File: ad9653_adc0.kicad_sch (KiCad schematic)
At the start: 20 parts, among them J201 142-0701-201, J202 142-0701-201, J203 142-0701-201, J204 142-0701-201, U201 AD9653BCPZ-125

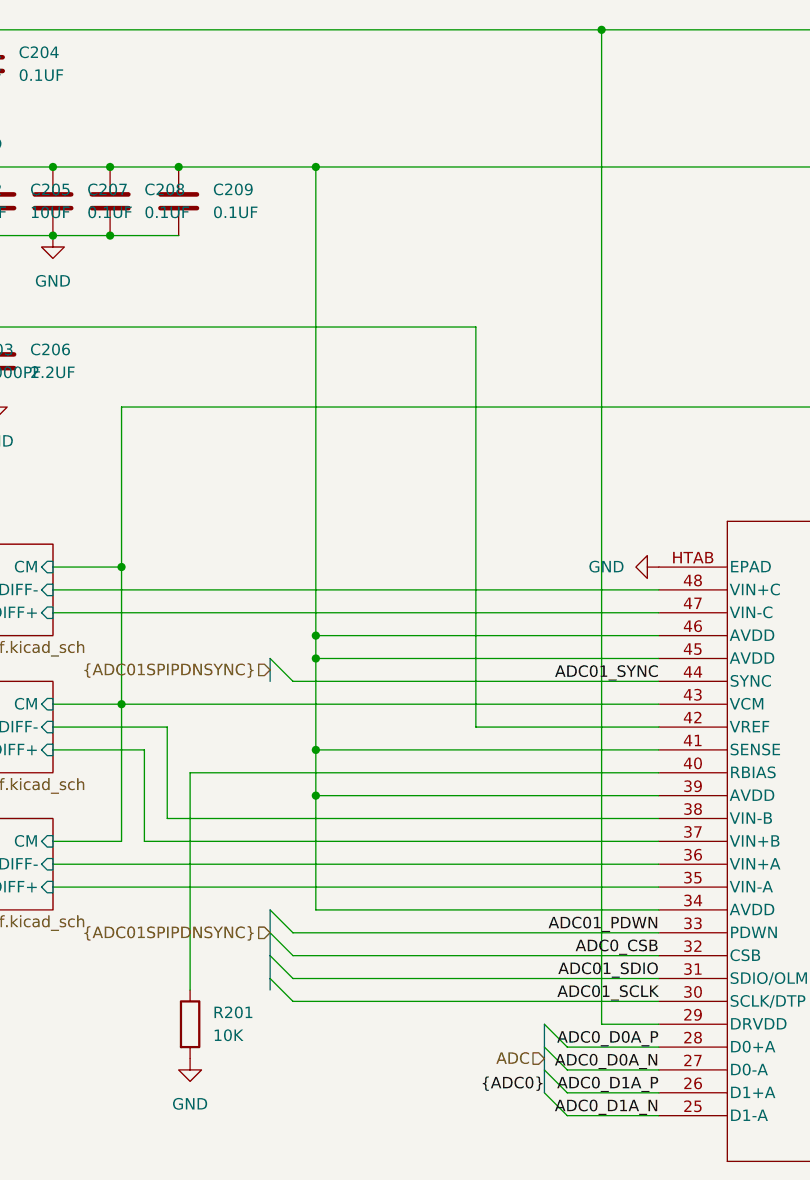
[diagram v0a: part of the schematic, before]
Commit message: Updates from Michal to fix ERC errors
Still lots of ERC warnings
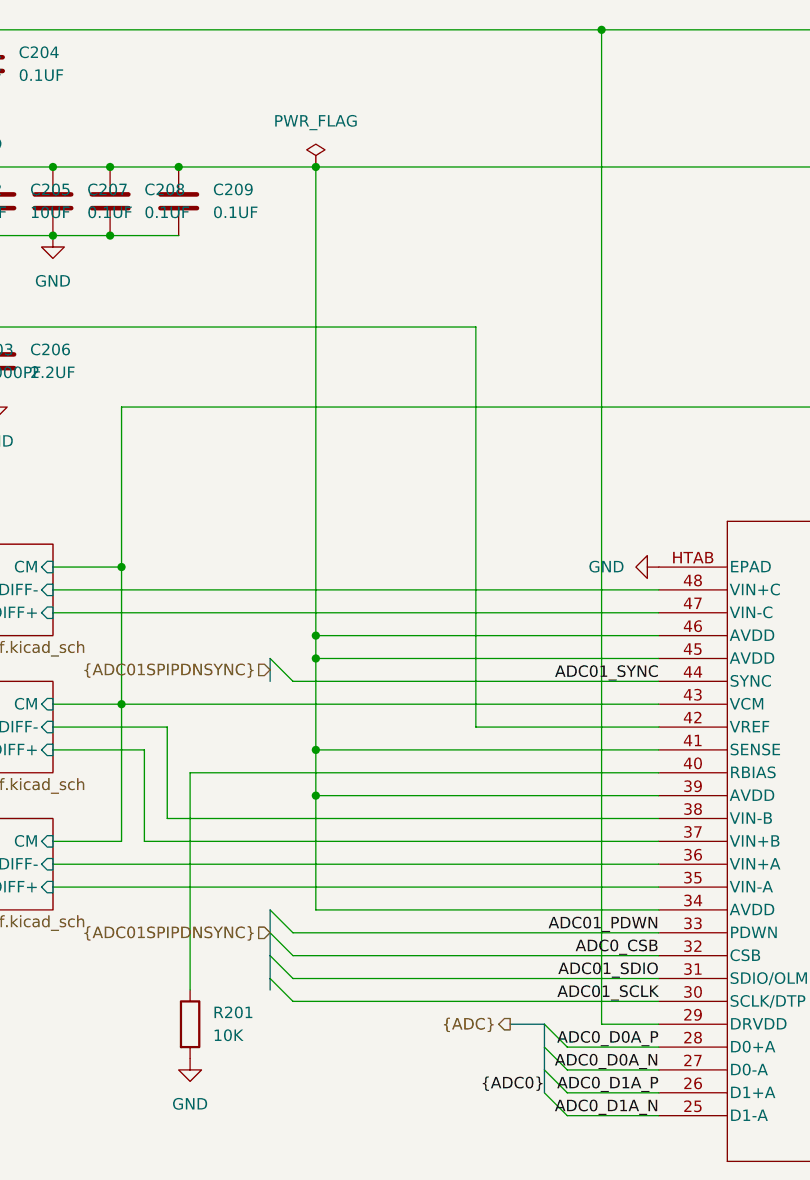
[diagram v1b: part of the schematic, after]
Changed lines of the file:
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@@
+		)
+	)
+	(bus
+		(pts
+			(xy 115.57 137.16) (xy 115.57 139.7)
+		)
+		(stroke
+			(width 0)
+			(type default)
 		)
 	)
@@
 	(bus
 		(pts
+			(xy 115.57 134.62) (xy 115.57 137.16)
+		)
+		(stroke
+			(width 0)
+			(type default)
+		)
+	)
+	(bus
+		(pts
 			(xy 233.68 121.92) (xy 233.68 124.46)
 		)
@@
 		)
 	)
+	(wire
+		(pts
+			(xy 200.66 39.37) (xy 90.17 39.37)
+		)
+		(stroke
+			(width 0)
+			(type default)
+		)
+	)
+	(wire
+		(pts
+			(xy 199.39 109.22) (xy 231.14 109.22)
+		)
+		(stroke
+			(width 0)
+			(type default)
+		)
+	)
+	(wire
+		(pts
+			(xy 238.76 66.04) (xy 238.76 81.28)
+		)
+		(stroke
+			(width 0)
+			(type default)
+		)
+	)
+	(wire
+		(pts
+			(xy 87.63 124.46) (xy 128.27 124.46)
+		)
+		(stroke
+			(width 0)
+			(type default)
+		)
+	)
+	(wire
+		(pts
+			(xy 76.2 106.68) (xy 76.2 130.81)
+		)
+		(stroke
+			(width 0)
+			(type default)
+		)
+	)
+	(wire
+		(pts
+			(xy 219.71 99.06) (xy 234.95 99.06)
+		)
+		(stroke
+			(width 0)
+			(type default)
+		)
+	)
+	(wire
+		(pts
+			(xy 60.96 114.3) (xy 68.58 114.3)
+		)
+		(stroke
+			(width 0)
+			(type default)
+		)
+	)
+	(wire
+		(pts
+			(xy 60.96 46.99) (xy 67.31 46.99)
+		)
+		(stroke
+			(width 0)
+			(type default)
+		)
+	)
+	(wire
+		(pts
+			(xy 87.63 129.54) (xy 128.27 129.54)
+		)
+		(stroke
+			(width 0)
+			(type default)
+		)
+	)
+	(wire
+		(pts
+			(xy 199.39 142.24) (xy 231.14 142.24)
+		)
+		(stroke
+			(width 0)
+			(type default)
+		)
+	)
+	(wire
+		(pts
+			(xy 90.17 93.98) (xy 128.27 93.98)
+		)
+		(stroke
+			(width 0)
+			(type default)
+		)
+	)
+	(wire
+		(pts
+			(xy 74.93 39.37) (xy 90.17 39.37)
+		)
+		(stroke
+			(width 0)
+			(type default)
+		)
+	)
+	(wire
+		(pts
+			(xy 67.31 46.99) (xy 74.93 46.99)
+		)
+		(stroke
+			(width 0)
+			(type default)
+		)
+	)
+	(wire
+		(pts
+			(xy 90.17 93.98) (xy 90.17 104.14)
+		)
+		(stroke
+			(width 0)
+			(type default)
+		)
+	)
 	(bus
 		(pts
-			(xy 115.57 134.62) (xy 115.57 137.16)
+			(xy 233.68 127) (xy 233.68 129.54)
+		)
+		(stroke
+			(width 0)
+			(type default)
+		)
+	)
+	(wire
+		(pts
+			(xy 60.96 119.38) (xy 128.27 119.38)
+		)
+		(stroke
+			(width 0)
+			(type default)
+		)
+	)
+	(wire
+		(pts
+			(xy 60.96 101.6) (xy 73.66 101.6)
+		)
+		(stroke
+			(width 0)
+			(type default)
+		)
+	)
+	(wire
+		(pts
+			(xy 199.39 124.46) (xy 231.14 124.46)
+		)
+		(stroke
+			(width 0)
+			(type default)
+		)
+	)
+	(wire
+		(pts
+			(xy 107.95 101.6) (xy 128.27 101.6)
+		)
+		(stroke
+			(width 0)
+			(type default)
+		)
+	)
+	(wire
+		(pts
+			(xy 90.17 109.22) (xy 128.27 109.22)
 		)
 		(stroke
@@
 	(bus
 		(pts
-			(xy 115.57 137.16) (xy 115.57 139.7)
-		)
-		(stroke
-			(width 0)
-			(type default)
-		)
-	)
-	(wire
-		(pts
-			(xy 200.66 39.37) (xy 90.17 39.37)
-		)
-		(stroke
-			(width 0)
-			(type default)
-		)
-	)
-	(wire
-		(pts
-			(xy 199.39 109.22) (xy 231.14 109.22)
-		)
-		(stroke
-			(width 0)
-			(type default)
-		)
-	)
-	(wire
-		(pts
-			(xy 238.76 66.04) (xy 238.76 81.28)
-		)
-		(stroke
-			(width 0)
-			(type default)
-		)
-	)
-	(wire
-		(pts
-			(xy 87.63 124.46) (xy 128.27 124.46)
-		)
-		(stroke
-			(width 0)
-			(type default)
-		)
-	)
-	(wire
-		(pts
-			(xy 76.2 106.68) (xy 76.2 130.81)
-		)
-		(stroke
-			(width 0)
-			(type default)
-		)
-	)
-	(wire
-		(pts
-			(xy 219.71 99.06) (xy 234.95 99.06)
-		)
-		(stroke
-			(width 0)
-			(type default)
-		)
-	)
-	(wire
-		(pts
-			(xy 60.96 114.3) (xy 68.58 114.3)
-		)
-		(stroke
-			(width 0)
-			(type default)
-		)
-	)
-	(wire
-		(pts
-			(xy 60.96 46.99) (xy 67.31 46.99)
-		)
-		(stroke
-			(width 0)
-			(type default)
-		)
-	)
-	(wire
-		(pts
-			(xy 87.63 129.54) (xy 128.27 129.54)
-		)
-		(stroke
-			(width 0)
-			(type default)
-		)
-	)
-	(wire
-		(pts
-			(xy 199.39 142.24) (xy 231.14 142.24)
-		)
-		(stroke
-			(width 0)
-			(type default)
-		)
-	)
-	(wire
-		(pts
-			(xy 90.17 93.98) (xy 128.27 93.98)
-		)
-		(stroke
-			(width 0)
-			(type default)
-		)
-	)
-	(wire
-		(pts
-			(xy 74.93 39.37) (xy 90.17 39.37)
-		)
-		(stroke
-			(width 0)
-			(type default)
-		)
-	)
-	(wire
-		(pts
-			(xy 67.31 46.99) (xy 74.93 46.99)
-		)
-		(stroke
-			(width 0)
-			(type default)
-		)
-	)
-	(wire
-		(pts
-			(xy 90.17 93.98) (xy 90.17 104.14)
-		)
-		(stroke
-			(width 0)
-			(type default)
-		)
-	)
-	(bus
-		(pts
-			(xy 233.68 127) (xy 233.68 129.54)
-		)
-		(stroke
-			(width 0)
-			(type default)
-		)
-	)
-	(wire
-		(pts
-			(xy 60.96 119.38) (xy 128.27 119.38)
-		)
-		(stroke
-			(width 0)
-			(type default)
-		)
-	)
-	(wire
-		(pts
-			(xy 60.96 101.6) (xy 73.66 101.6)
-		)
-		(stroke
-			(width 0)
-			(type default)
-		)
-	)
-	(wire
-		(pts
-			(xy 199.39 124.46) (xy 231.14 124.46)
-		)
-		(stroke
-			(width 0)
-			(type default)
-		)
-	)
-	(wire
-		(pts
-			(xy 107.95 101.6) (xy 128.27 101.6)
-		)
-		(stroke
-			(width 0)
-			(type default)
-		)
-	)
-	(wire
-		(pts
-			(xy 90.17 109.22) (xy 128.27 109.22)
+			(xy 111.76 134.62) (xy 115.57 134.62)
 		)
 		(stroke
@@
 		)
 	)
-	(hierarchical_label "ADC"
-		(shape input)
-		(at 115.57 138.43 180)
+	(hierarchical_label "{ADC}"
+		(shape output)
+		(at 111.76 134.62 180)
 		(fields_autoplaced yes)
 		(effects
@@
 					(unit 1)
 				)
+			)
+		)
+	)
+	(symbol
+		(lib_id "power:PWR_FLAG")
+		(at 90.17 39.37 0)
+		(unit 1)
+		(exclude_from_sim no)
+		(in_bom yes)
+		(on_board yes)
+		(dnp no)
+		(fields_autoplaced yes)
+		(property "Reference" "#FLG05"
+			(at 90.17 37.465 0)
+			(effects
+				(font
+					(size 1.27 1.27)
+				)
+				(hide yes)
+			)
+		)
+		(property "Value" "PWR_FLAG"
+			(at 90.17 34.29 0)
+			(effects
+				(font
+					(size 1.27 1.27)
+				)
+			)
+		)
+		(property "Footprint" ""
+			(at 90.17 39.37 0)
+			(effects
+				(font
+					(size 1.27 1.27)
+				)
+				(hide yes)
+			)
+		)
+		(property "Datasheet" "~"
+			(at 90.17 39.37 0)
+			(effects
+				(font
+					(size 1.27 1.27)
+				)
+				(hide yes)
+			)
+		)
+		(property "Description" "Special symbol for telling ERC where power comes from"
+			(at 90.17 39.37 0)
+			(effects
+				(font
+					(size 1.27 1.27)
+				)
+				(hide yes)
+			)
+		)
+		(pin "1"
+		)
+		(instances
+			(project "zest"
+				(path "/00000000-0000-0000-0000-000000000003/00000000-0000-0000-0000-000000000000"
+					(reference "#FLG05")
+					(unit 1)
+				)

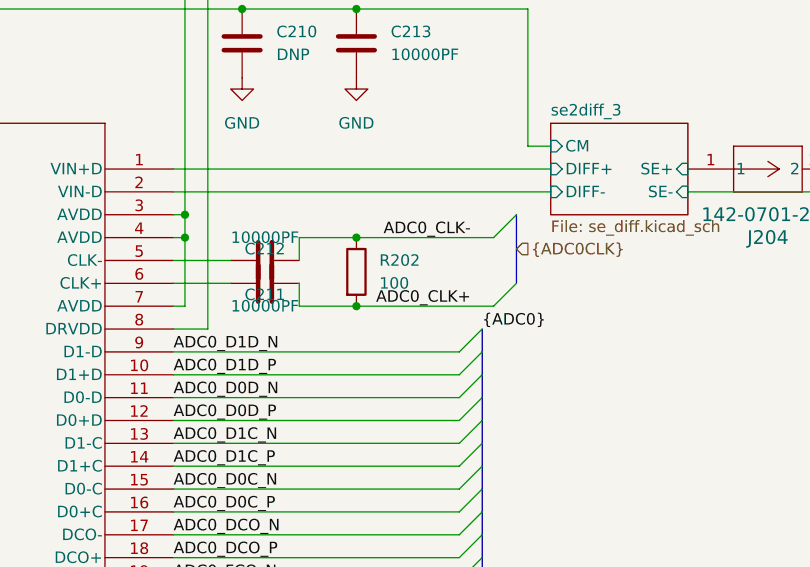
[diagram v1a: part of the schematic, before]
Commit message: Schematic Changes
Added Manufacturer/MPN/Description Fields to parts
Added libraries to project
Modified FMC schematic to use new symbol
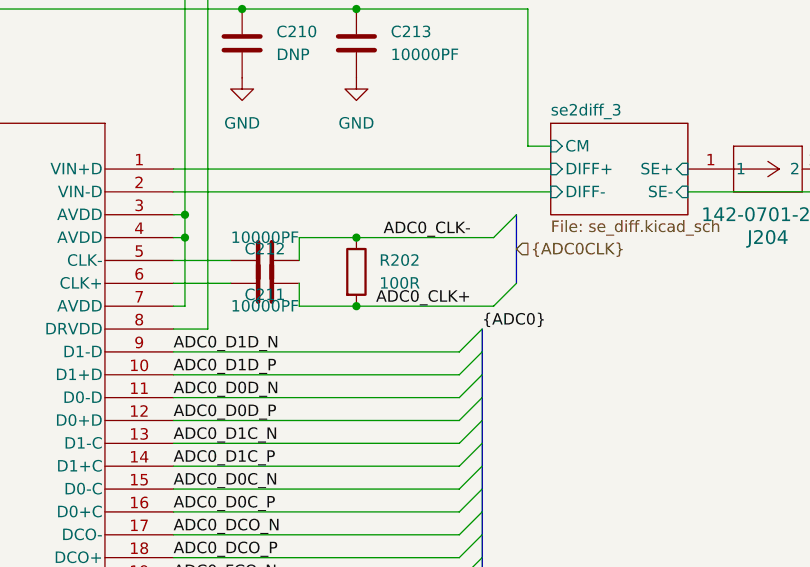
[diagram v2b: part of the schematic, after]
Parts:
- C201, C205: Manufacturer (none) -> TDK; Manufacturer Part Number (none) -> C1608X5R1A106M080AC
- C202, C204, C207, C208, C209: Manufacturer (none) -> Murata; Manufacturer Part Number (none) -> GRM155R61A104KA01D
- C203, C211, C212, C213: Manufacturer (none) -> TDK; Manufacturer Part Number (none) -> C1608C0G1E103J080AA
- C206: Manufacturer (none) -> Kyocera AVX; Manufacturer Part Number (none) -> F381A225MMA
- J201, J202, J203, J204: Manufacturer (none) -> Cinch; Manufacturer Part Number (none) -> 142-0701-201
- R201: Manufacturer (none) -> Vishay; Manufacturer Part Number (none) -> MCT0603MD1002DP500
- R202: value 100 -> 100R; Manufacturer (none) -> YAGEO; Manufacturer Part Number (none) -> RC0603FR-07100RL
- U201: Manufacturer (none) -> Analog Devices; Manufacturer Part Number (none) -> AD9653BCPZ-125

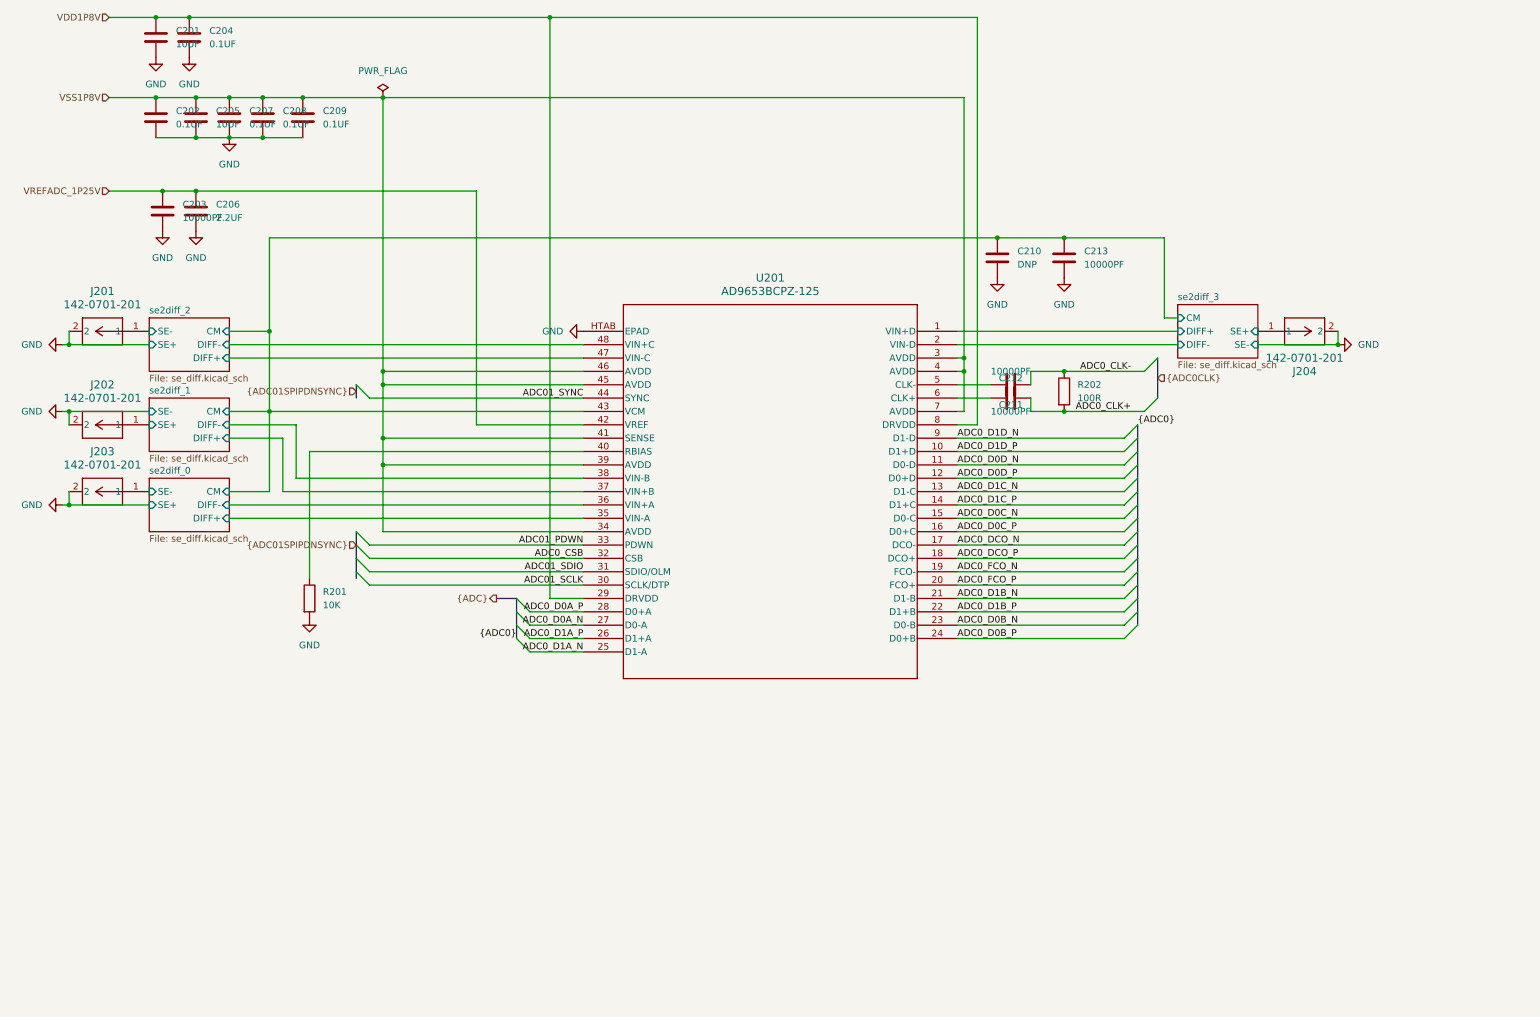
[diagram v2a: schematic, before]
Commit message: Schematics update
Cleaned up RF ADC and front end sections.
Verified that changes did not changes anything about the layout.
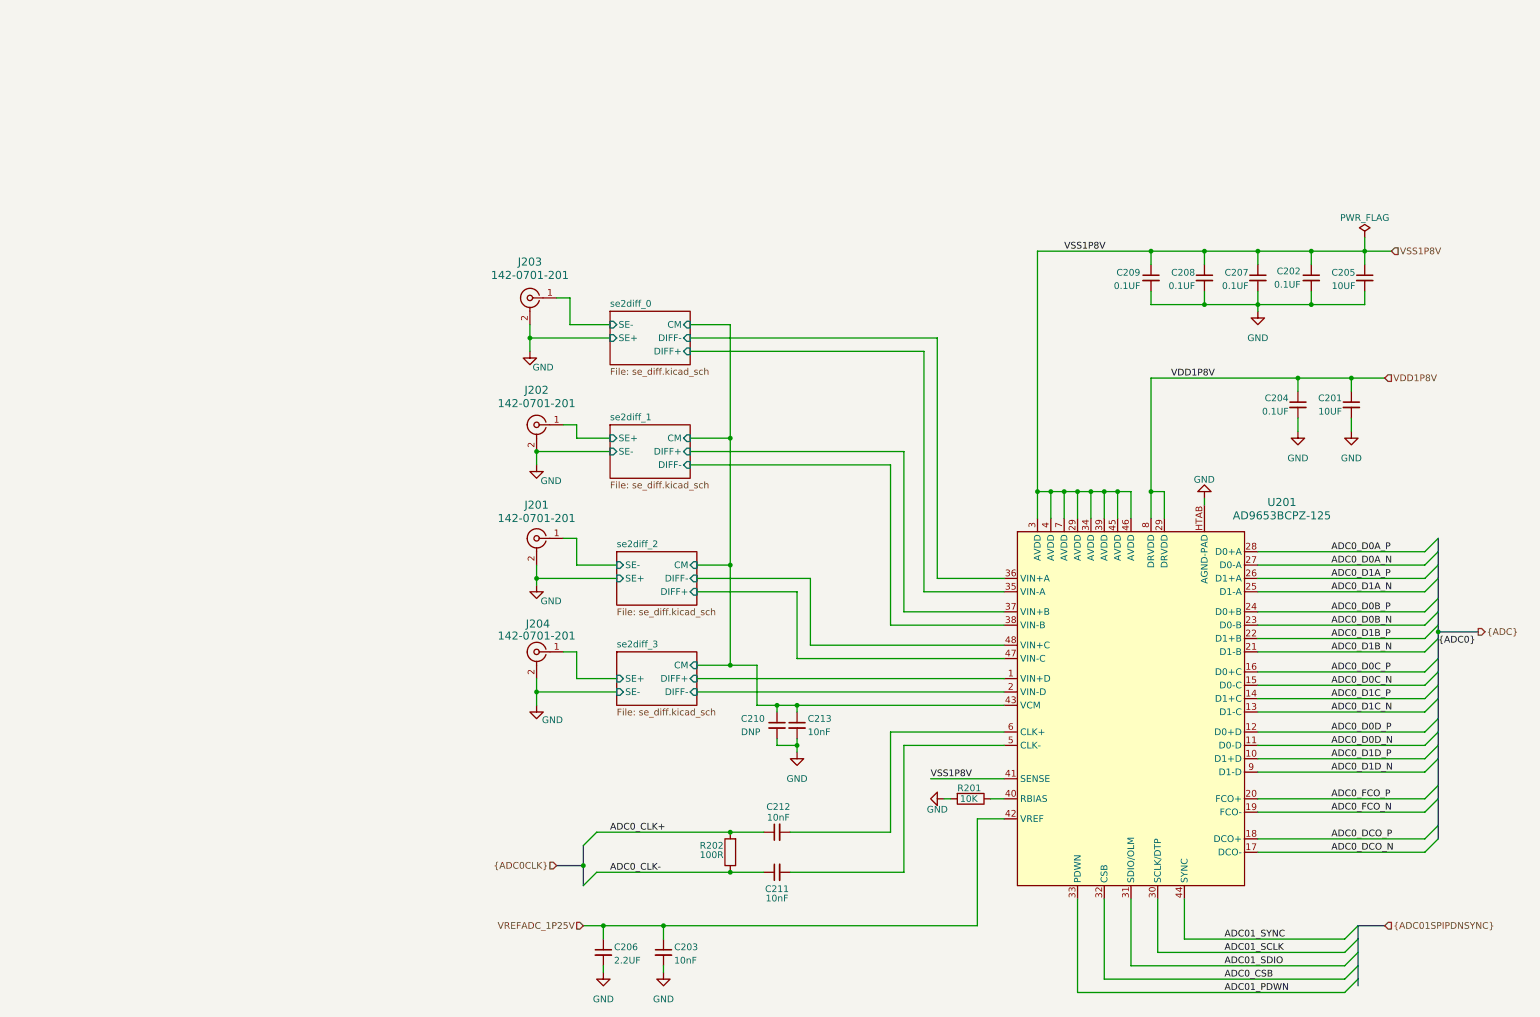
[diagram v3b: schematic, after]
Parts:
- C201, C202, C204, C205, C206, C207, C208, C209, C210: symbol Device:C -> Device:C_Small
- C203, C211, C212, C213: value 10000PF -> 10nF; symbol Device:C -> Device:C_Small
- J201, J202, J203, J204: symbol 001_symbol:142-0701-201_GH -> Zest_Custom:SMA_Coaxial
- U201: symbol 001_symbol:AD9653BCPZ-125 -> Zest_Custom:AD9653
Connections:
- net VSS1P8V: now also U201.29 (DRVDD)
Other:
- moved on the sheet: C201, C202, C203, C204, C205, C206, C207, C208, C209, C210, C211, C212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

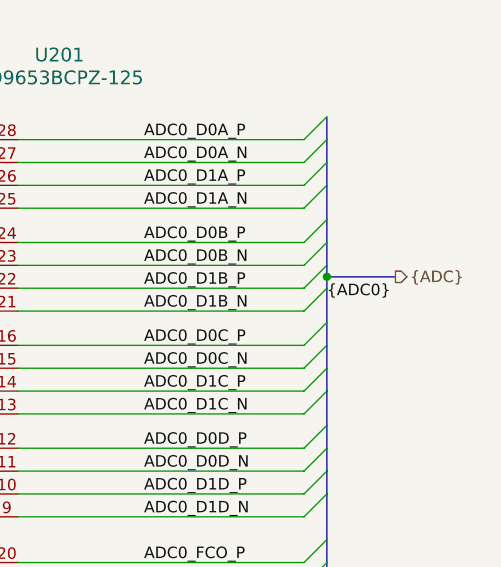
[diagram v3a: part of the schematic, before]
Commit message: Updated some Schematics
- updated slowmon schematic
- updated diff to se schematic
- cleaned up DRC/ERC errors
No changes were made that effected the PCB layout
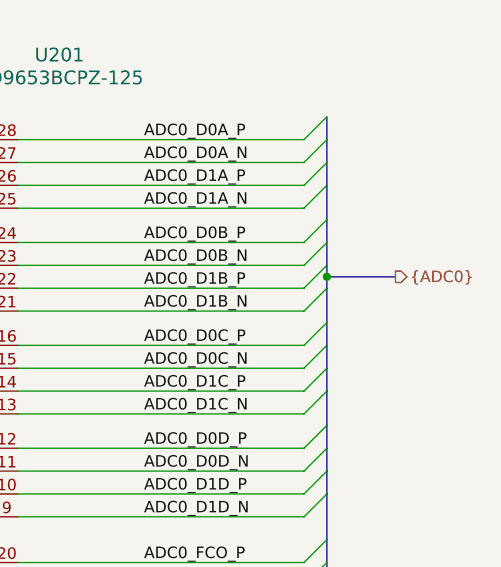
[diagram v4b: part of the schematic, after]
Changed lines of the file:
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@@
-		)
-	)
-	(label "{ADC0}"
-		(at 290.83 143.51 0)
-		(fields_autoplaced yes)
-		(effects
-			(font
-				(size 1.27 1.27)
-			)
-			(justify left bottom)
 		)
 	)
@@
 		)
 	)
-	(hierarchical_label "{ADC}"
+	(hierarchical_label "{ADC0}"
 		(shape output)
 		(at 298.45 140.97 0)
